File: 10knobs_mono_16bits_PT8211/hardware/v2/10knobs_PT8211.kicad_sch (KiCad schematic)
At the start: 48 parts

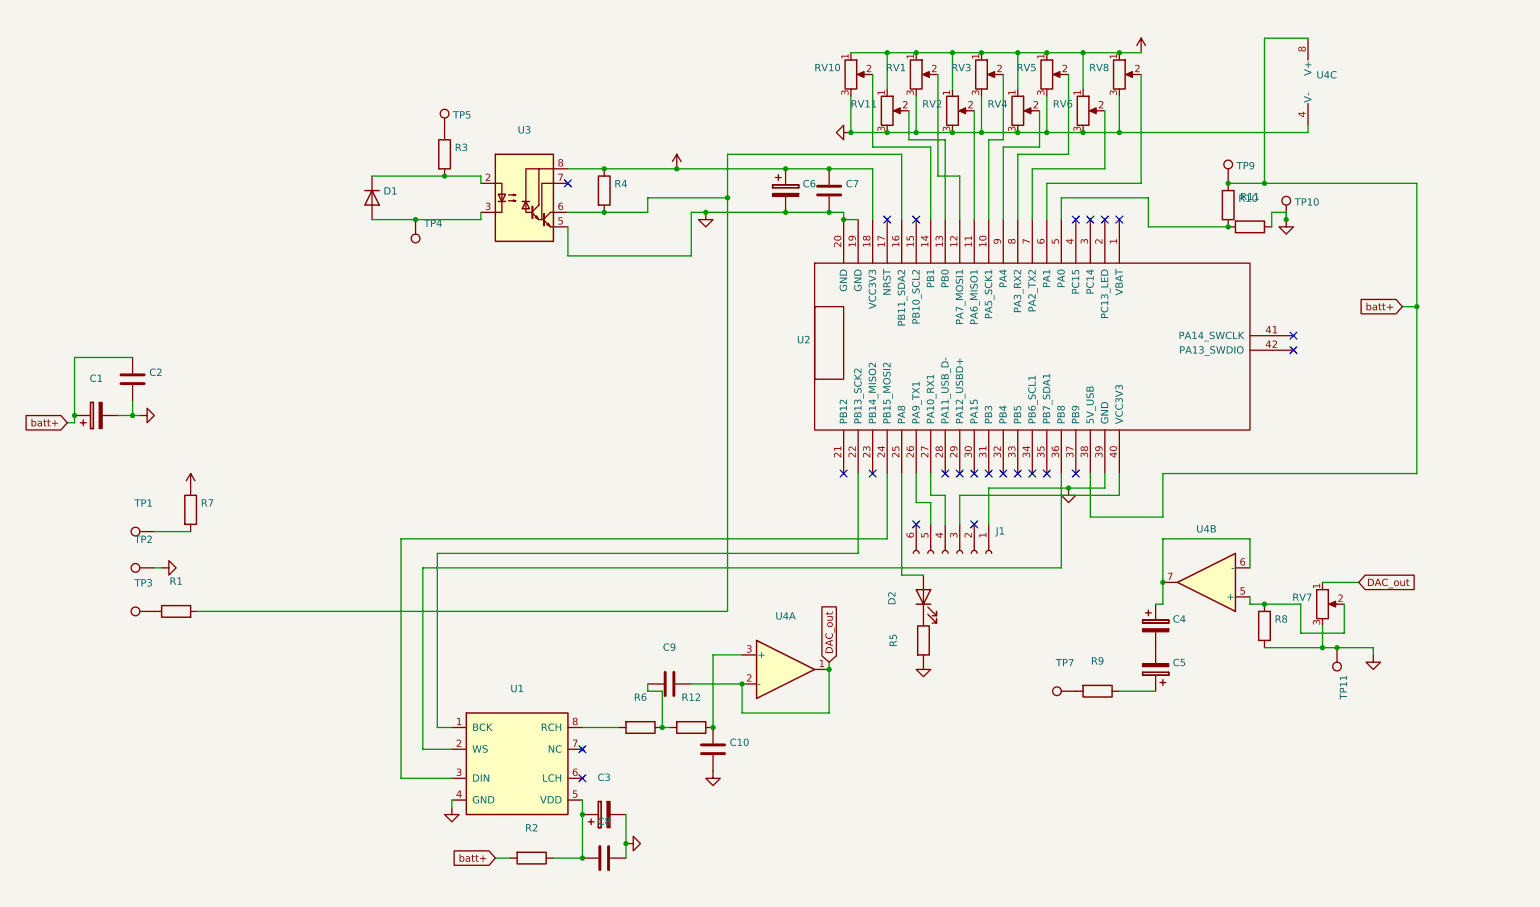
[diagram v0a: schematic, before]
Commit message: Moved to seperate folders
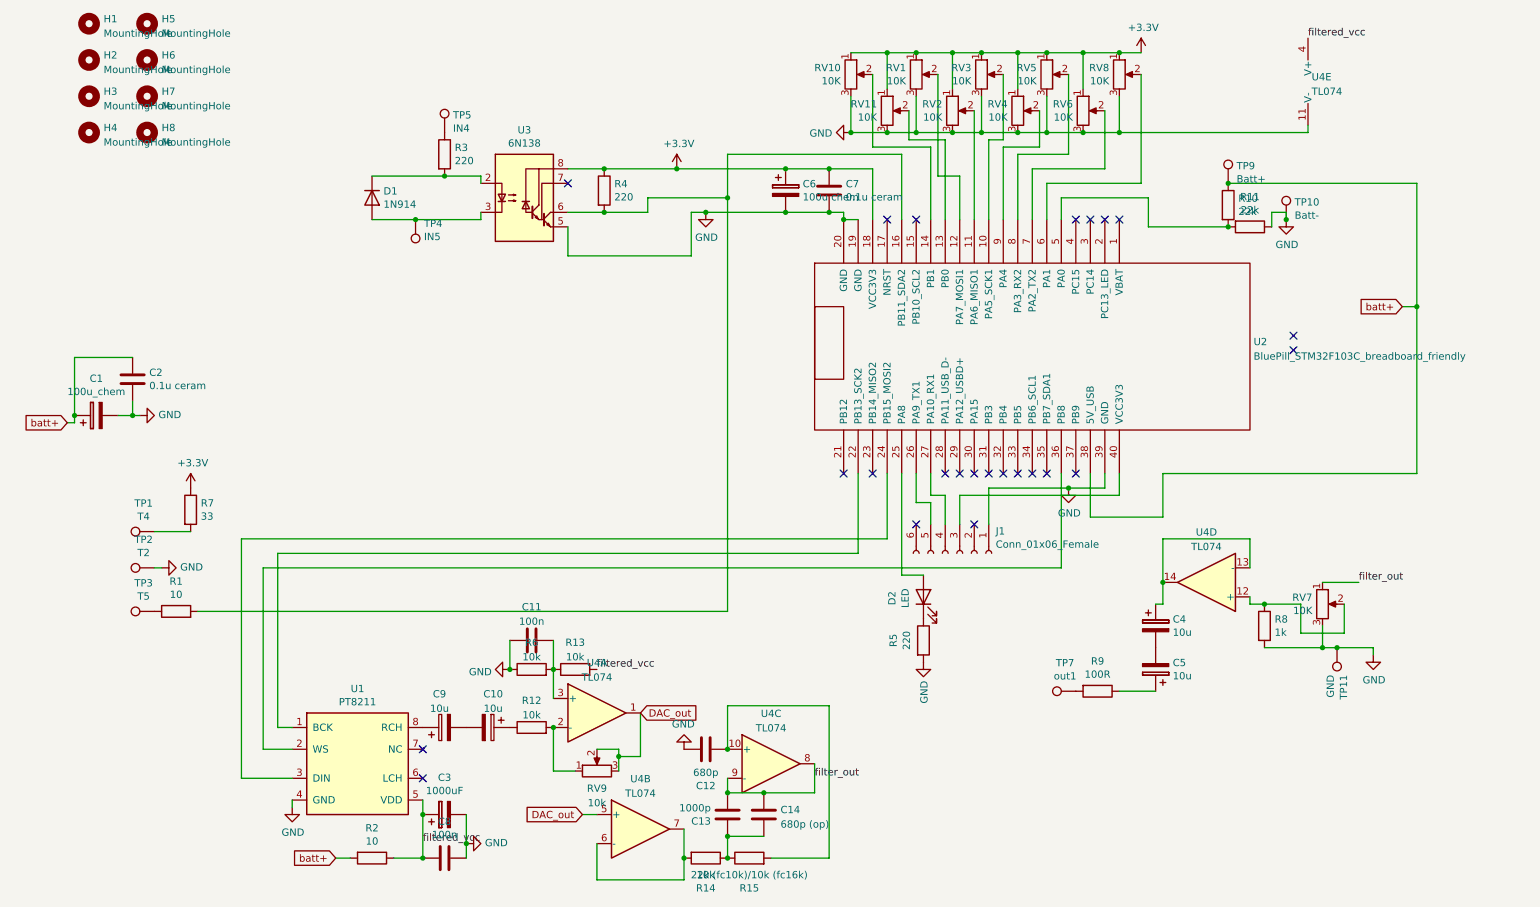
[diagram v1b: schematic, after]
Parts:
- removed C10, C9: (no value), symbol Device:C
- removed U2: (no value), symbol bluepill_breakouts:BluePill_STM32F103C
- removed U4: (no value), symbol Amplifier_Operational:LM358
- added C10, C9: 10u, Capacitor_THT:CP_Radial_D5.0mm_P2.50mm, symbol Device:C_Polarized
- added C11: 100n, Capacitor_THT:C_Disc_D4.7mm_W2.5mm_P5.00mm, symbol Device:C
- added C12: 680p, Capacitor_THT:C_Disc_D5.0mm_W2.5mm_P2.50mm, symbol Device:C
- added C13: 1000p, Capacitor_THT:C_Disc_D5.0mm_W2.5mm_P2.50mm, symbol Device:C
- added C14: 680p (op), Capacitor_THT:C_Disc_D3.8mm_W2.6mm_P2.50mm, symbol Device:C
- added H1, H2, H5, H8: MountingHole, MountingHole:MountingHole_3.2mm_M3, symbol Mechanical:MountingHole
- added H3, H4, H6, H7: MountingHole, MountingHole:MountingHole_3.2mm_M3_ISO7380_Pad, symbol Mechanical:MountingHole
- added R13, R14: 10k, Resistor_THT:R_Axial_DIN0207_L6.3mm_D2.5mm_P7.62mm_Horizontal, symbol Device:R
- added R15: 22k (fc10k)/10k (fc16k), Resistor_THT:R_Axial_DIN0207_L6.3mm_D2.5mm_P7.62mm_Horizontal, symbol Device:R
- added RV9: 10k, Potentiometer_THT:Potentiometer_Runtron_RM-065_Vertical, symbol Device:R_Potentiometer
- added U2: BluePill_STM32F103C_breadboard_friendly, BluePill_breakouts:BluePill_STM32F103C_breadboard_friendly, symbol bluepill_breakouts:BluePill_STM32F103C_breadboard_friendly
- added U4: TL074, Package_DIP:DIP-14_W7.62mm_Socket, symbol Amplifier_Operational:TL074
- C1: value (none) -> 100u_chem; footprint (none) -> Capacitor_THT:CP_Radial_D5.0mm_P2.50mm
- C2, C7: value (none) -> 0.1u ceram; footprint (none) -> Capacitor_THT:C_Disc_D3.0mm_W2.0mm_P2.50mm
- C3: value (none) -> 1000uF; footprint (none) -> Capacitor_THT:CP_Radial_D8.0mm_P3.50mm
- C4, C5: value (none) -> 10u; footprint (none) -> Capacitor_THT:CP_Radial_D5.0mm_P2.50mm
- C6: value (none) -> 100u chem; footprint (none) -> Capacitor_THT:CP_Radial_D5.0mm_P2.50mm
- C8: value (none) -> 100n; footprint (none) -> Capacitor_THT:C_Disc_D3.0mm_W2.0mm_P2.50mm
- D1: value (none) -> 1N914; footprint (none) -> Diode_THT:D_DO-35_SOD27_P7.62mm_Horizontal
- D2: value (none) -> LED; footprint (none) -> LED_THT:LED_D3.0mm
- J1: value (none) -> Conn_01x06_Female; footprint (none) -> Connector_PinHeader_2.54mm:PinHeader_1x06_P2.54mm_Vertical
- R1, R2: value (none) -> 10; footprint (none) -> Resistor_THT:R_Axial_DIN0207_L6.3mm_D2.5mm_P7.62mm_Horizontal
- R10, R11: value (none) -> 22k; footprint (none) -> Resistor_THT:R_Axial_DIN0207_L6.3mm_D2.5mm_P7.62mm_Horizontal
- R12, R6: value (none) -> 10k; footprint (none) -> Resistor_THT:R_Axial_DIN0207_L6.3mm_D2.5mm_P7.62mm_Horizontal
- R3, R4, R5: value (none) -> 220; footprint (none) -> Resistor_THT:R_Axial_DIN0207_L6.3mm_D2.5mm_P7.62mm_Horizontal
- R7: value (none) -> 33; footprint (none) -> Resistor_THT:R_Axial_DIN0207_L6.3mm_D2.5mm_P7.62mm_Horizontal
- R8: value (none) -> 1k; footprint (none) -> Resistor_THT:R_Axial_DIN0207_L6.3mm_D2.5mm_P7.62mm_Horizontal
- R9: value (none) -> 100R; footprint (none) -> Resistor_THT:R_Axial_DIN0207_L6.3mm_D2.5mm_P7.62mm_Horizontal
- RV1, RV10, RV11, RV2, RV3, RV4, RV5, RV6, RV7, RV8: value (none) -> 10K; footprint (none) -> Potentiometer_THT:Potentiometer_Alps_RK09K_Single_Vertical
- TP1: value (none) -> T4; footprint (none) -> TestPoint:TestPoint_THTPad_2.5x2.5mm_Drill1.2mm
- TP10: value (none) -> Batt-; footprint (none) -> TestPoint:TestPoint_THTPad_2.5x2.5mm_Drill1.2mm
- TP11: value (none) -> GND; footprint (none) -> TestPoint:TestPoint_THTPad_2.5x2.5mm_Drill1.2mm
- TP2: value (none) -> T2; footprint (none) -> TestPoint:TestPoint_THTPad_2.5x2.5mm_Drill1.2mm
- TP3: value (none) -> T5; footprint (none) -> TestPoint:TestPoint_THTPad_2.5x2.5mm_Drill1.2mm
- TP4: value (none) -> IN5; footprint (none) -> TestPoint:TestPoint_THTPad_2.5x2.5mm_Drill1.2mm
- TP5: value (none) -> IN4; footprint (none) -> TestPoint:TestPoint_THTPad_2.5x2.5mm_Drill1.2mm
- TP7: value (none) -> out1; footprint (none) -> TestPoint:TestPoint_THTPad_2.5x2.5mm_Drill1.2mm
- TP9: value (none) -> Batt+; footprint (none) -> TestPoint:TestPoint_THTPad_2.5x2.5mm_Drill1.2mm
- U1: value (none) -> PT8211
- U3: value (none) -> 6N138; footprint (none) -> Package_DIP:DIP-8_W7.62mm
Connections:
- net +3V3: now also U2.18 (VCC3V3)
- net DAC_out: now also RV9.2, RV9.3, U4.1, U4.5 (+); no longer RV7.1
- net GND: now also R6.1, C11.1, C12.1, U2.19 (GND), U2.20 (GND), U2.39 (GND), U4.11 (V-)
- net batt+: now also U2.38 (5V_USB)
- net at RV3.2: now also U2.10 (PA5_SCK1)
- net at RV2.2: now also U2.11 (PA6_MISO1)
- net at RV1.2: now also U2.12 (PA7_MOSI1)
- net at RV11.2: now also U2.13 (PB0)
- net at RV10.2: now also U2.14 (PB1)
- net at R1.2, R4.2, U3.6 (VO2): now also U2.16 (PB11_SDA2)
- net at U1.1 (BCK): now also U2.22 (PB13_SCK2)
- net at U1.3 (DIN): now also U2.24 (PB15_MOSI2)
- net at D2.2 (A): now also U2.25 (PA8)
- net at J1.5 (Pin_5): now also U2.26 (PA9_TX1)
- net at J1.4 (Pin_4): now also U2.27 (PA10_RX1)
- net at U1.2 (WS): now also U2.36 (PB8)
- net at J1.3 (Pin_3): now also U2.40 (VCC3V3)
- net at R10.2, R11.2: now also U2.5 (PA0)
- net at RV8.2: now also U2.6 (PA1)
- net at RV6.2: now also U2.7 (PA2_TX2)
- net at RV5.2: now also U2.8 (PA3_RX2)
- net at RV4.2: now also U2.9 (PA4)
- net at R8.1, RV7.2: now also U4.12 (+)
- net at R12.1: now also C10.1
- net at C4.1: now also U4.13 (-), U4.14
- net filtered_vcc: now reaches C3.1, C8.2, R2.1, U1.5 (VDD)
- net filtered_vcc: now also R13.2, U4.4 (V+)
- net at U1.8 (RCH): now also C9.1; no longer R6.2
- net at R12.2: now also RV9.1, U4.2 (-); no longer R6.1
- new net: C12.2, R15.2, U4.10 (+)
- new net: C13.1, C14.2, R14.1, R15.1
- new net: R14.2, U4.6 (-), U4.7
- new net: C10.2, C9.2
- new net: C11.2, R13.1, R6.2, U4.3 (+)
- new net filter_out: C13.2, C14.1, RV7.1, U4.8, U4.9 (-)
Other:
- moved on the sheet: C3, C8, R2, U1

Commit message: Fixed static allocation of oscillators
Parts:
- U1: footprint (none) -> Package_SO:SOP-8_3.9x4.9mm_P1.27mm
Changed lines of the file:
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@@
     (property "Reference" "U1" (id 0) (at 88.9 162.1282 0))
     (property "Value" "PT8211" (id 1) (at 88.9 164.4396 0))
-    (property "Footprint" "" (id 2) (at 88.9 175.26 0)
+    (property "Footprint" "Package_SO:SOP-8_3.9x4.9mm_P1.27mm" (id 2) (at 88.9 175.26 0)
       (effects (font (size 1.27 1.27) italic) hide)
     )
